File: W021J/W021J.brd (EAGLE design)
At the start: 18.4 x 62.1 mm, 2 parts, among them J1 503480-1800

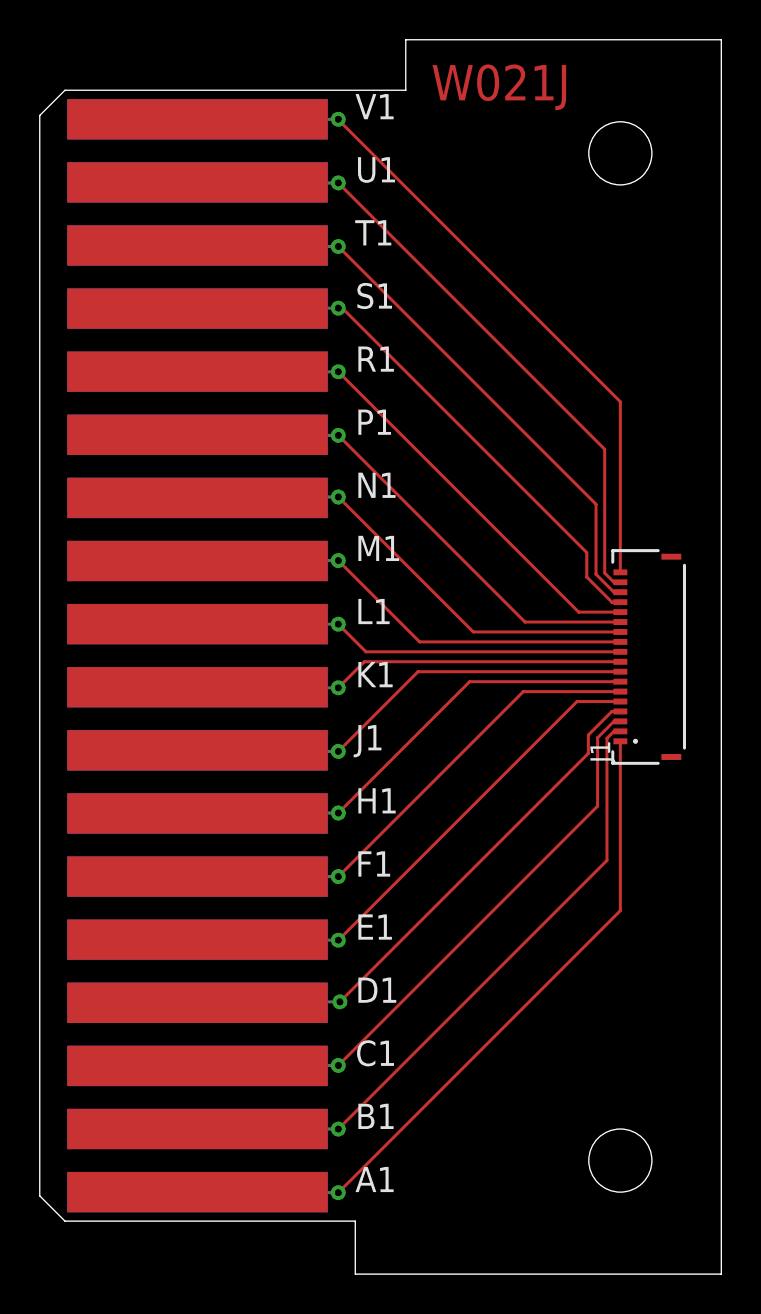
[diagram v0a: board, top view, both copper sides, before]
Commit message: Added bypass capacitors, reworked W021J
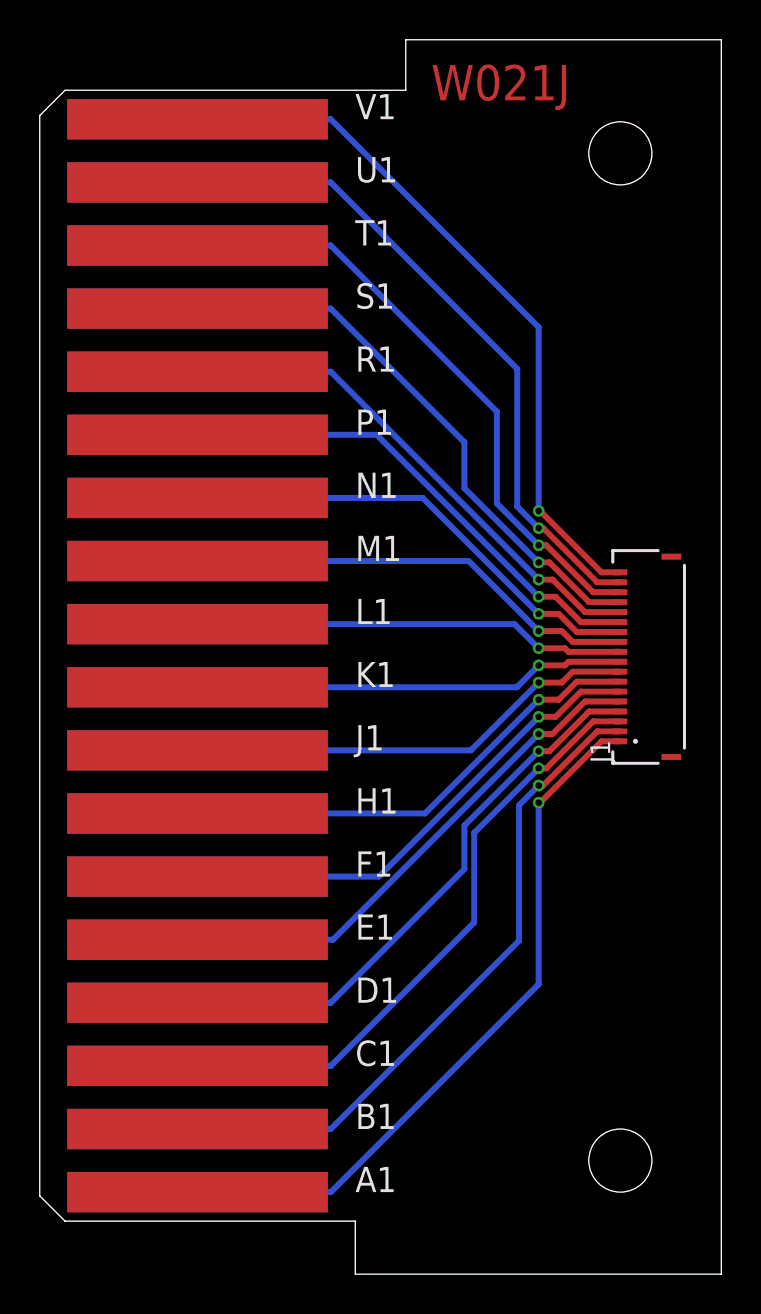
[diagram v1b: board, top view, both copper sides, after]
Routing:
- net N$4: track 27.9 -> 28.6 mm
- net N$7: track 30.6 -> 31.2 mm
- net N$3: track 30.5 -> 31.1 mm
- net N$8: track 28.1 -> 28.7 mm

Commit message: Disable thermals on pours to work around EAGLE bug
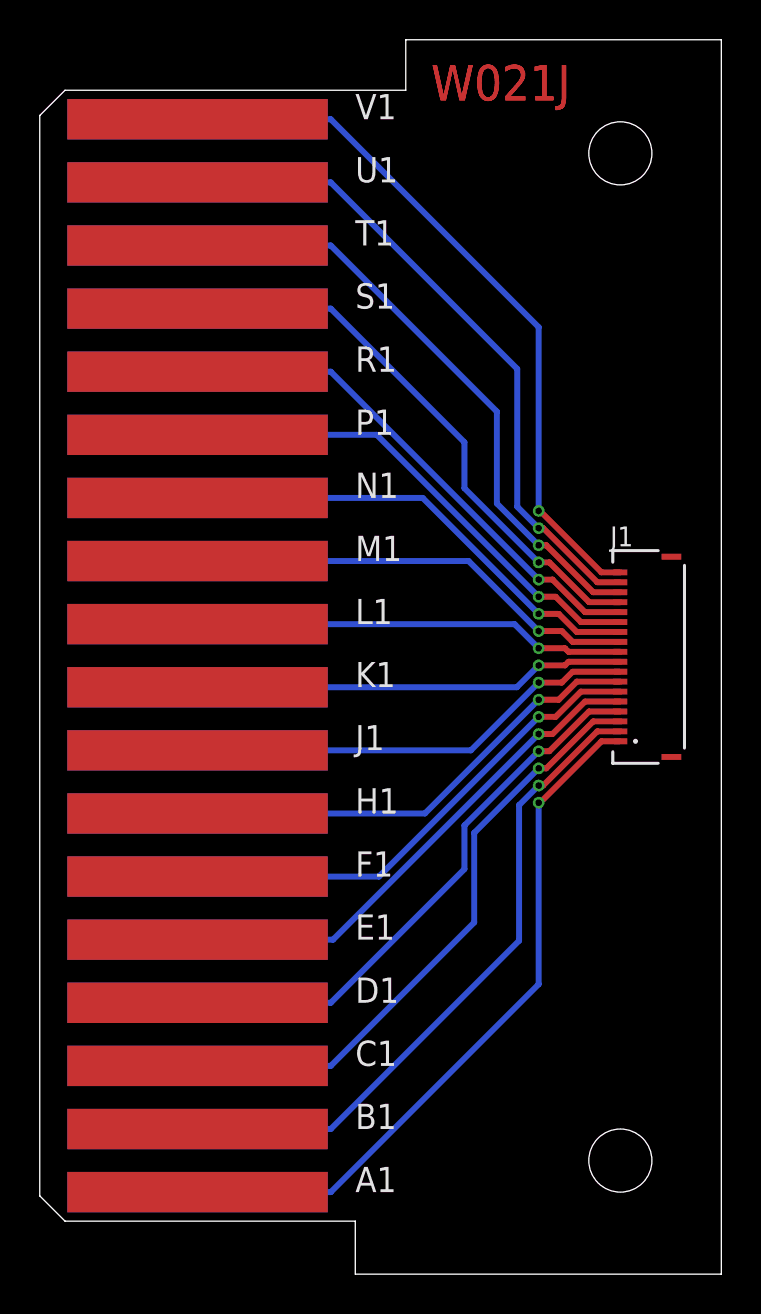
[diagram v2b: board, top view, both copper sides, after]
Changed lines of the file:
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@@
 <layer number="27" name="tValues" color="7" fill="1" visible="no" active="yes"/>
 <layer number="28" name="bValues" color="7" fill="1" visible="no" active="yes"/>
-<layer number="29" name="tStop" color="7" fill="3" visible="no" active="yes"/>
+<layer number="29" name="tStop" color="7" fill="3" visible="yes" active="yes"/>
 <layer number="30" name="bStop" color="7" fill="6" visible="no" active="yes"/>
 <layer number="31" name="tCream" color="7" fill="4" visible="no" active="yes"/>
@@
 <text x="19.69" y="60.83" size="1.778" layer="1" font="vector" ratio="15" rot="SR0" align="top-left">W021J</text>
 <text x="19.69" y="60.83" size="1.778" layer="29" font="vector" ratio="15" rot="SR0" align="top-left">W021J</text>
+<text x="19.69" y="60.83" size="1.778" layer="1" font="vector" ratio="15" rot="SR0" align="top-left">W021J</text>
 </plain>
 <attributes>
@@
 <attribute name="BUILT_BY" value="EMA_UL_Team" x="33.02" y="69.9888" size="1.778" layer="27" rot="R90" display="off"/>
 <attribute name="MANUFACTURER_PART_NUMBER" value="503480-0600" x="33.02" y="69.9888" size="1.778" layer="27" rot="R90" display="off"/>
-<attribute name="NAME" x="28.702" y="25.7166" size="1" layer="25" font="vector" rot="SR90"/>
+<attribute name="NAME" x="28.702" y="36.6166" size="1" layer="25" font="vector" ratio="15" rot="SR0"/>
 <attribute name="VENDOR" value="Molex Connector Corporation" x="33.02" y="69.9888" size="1.778" layer="27" rot="R90" display="off"/>
 </element>
@@
 <mfgpreviewcolor name="soldermaskcolor" color="0xC8FFFFFF"/>
 <mfgpreviewcolor name="silkscreencolor" color="0xFF000000"/>
-<mfgpreviewcolor name="backgroundcolor" color="0xFF000000"/>
-<mfgpreviewcolor name="coppercolor" color="0xFFFFBF00"/>
+<mfgpreviewcolor name="backgroundcolor" color="0xFF282828"/>
+<mfgpreviewcolor name="coppercolor" color="0xFFFFAA00"/>
 <mfgpreviewcolor name="substratecolor" color="0xFF786E46"/>
 </mfgpreviewcolors>
